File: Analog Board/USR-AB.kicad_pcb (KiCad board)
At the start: 2 copper layers, 81.3 x 8.9 mm, 6 parts, among them J2 S5B-XH-A_LF__SN_, J3 S5B-XH-A_LF__SN_, U2 CD74HC4067SM96, U3 SC0918

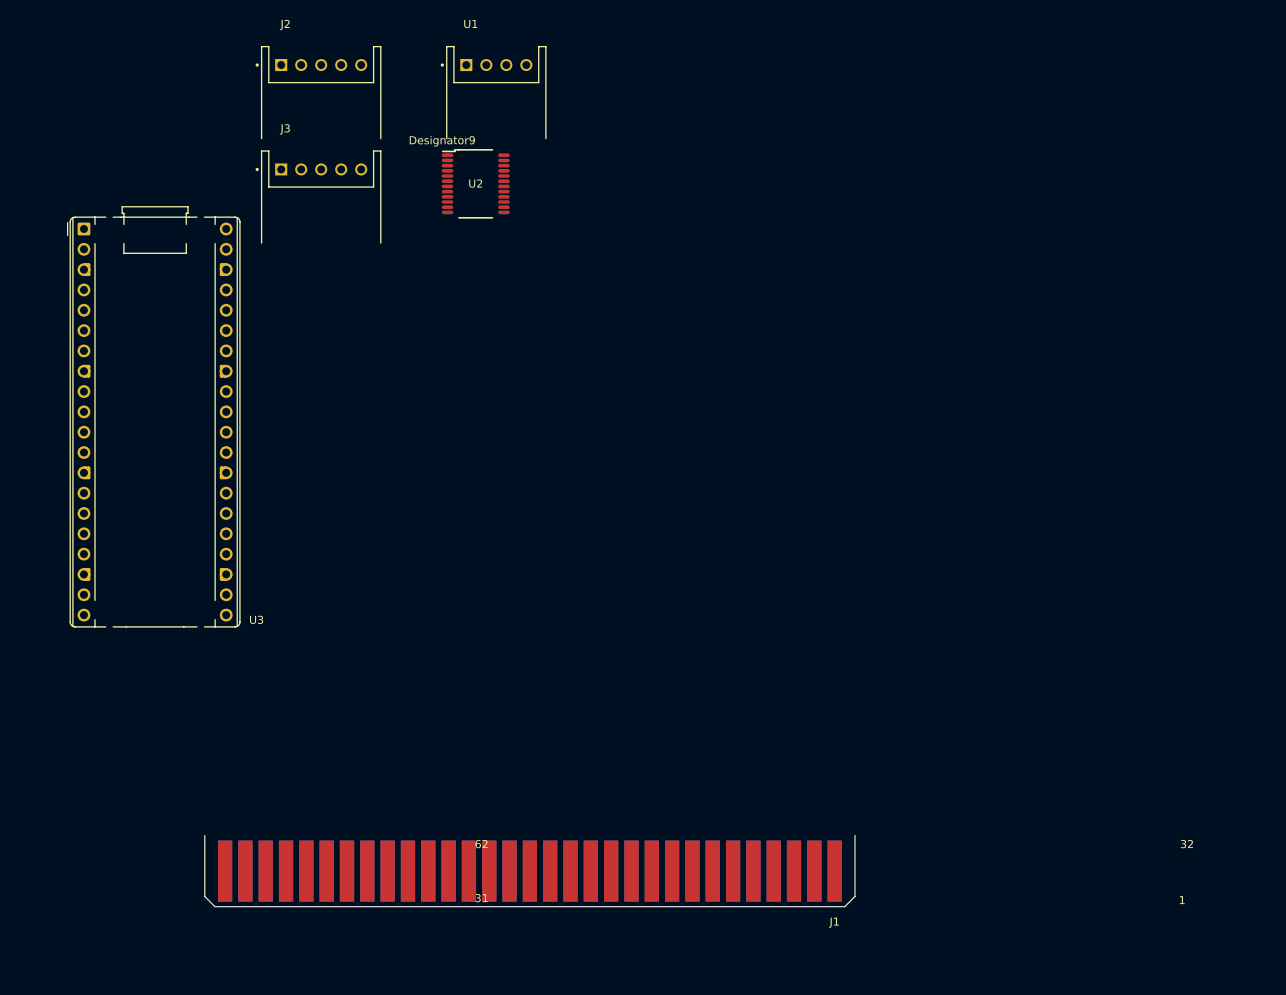
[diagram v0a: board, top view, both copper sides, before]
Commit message: updated Analog board PCB
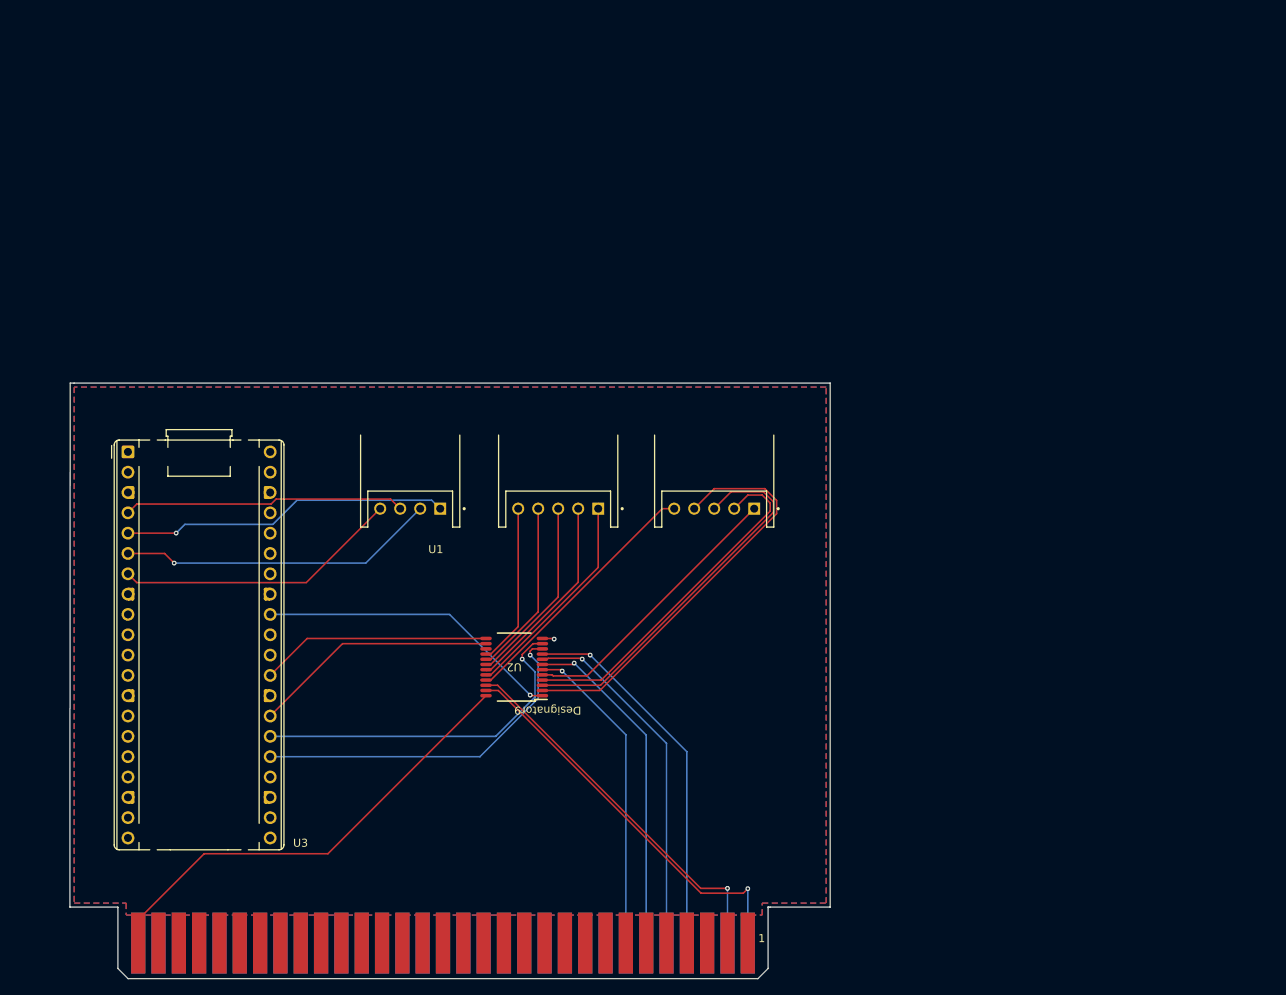
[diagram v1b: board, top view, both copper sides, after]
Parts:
- moved J2 66.0 mm to (125.5, 90.0), turned to 180 degrees
- moved U2 60.6 mm to (100.5, 115.5), turned to 180 degrees
- moved U1 45.4 mm to (87.5, 90.0), turned to 180 degrees
- moved J3 42.9 mm to (106.0, 90.0), turned to 180 degrees
- moved U3 28.4 mm to (52.2, 88.6)
- moved J1 14.1 mm to (129.7, 150.0)
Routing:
- net 5V: track 0.00 -> 58.0 mm
- net M4_THERM: track 0.00 -> 52.6 mm
- net DRIVE1_HE: track 0.00 -> 50.3 mm, vias 0 -> 1
- net M3_THERM: track 0.00 -> 48.5 mm
- net DRIVE2_HE: track 0.00 -> 47.5 mm, vias 0 -> 1
- net M1_CS: track 0.00 -> 47.0 mm, vias 0 -> 1
- net M2_CS: track 0.00 -> 44.9 mm, vias 0 -> 1
- net MUX_S0: track 0.00 -> 44.5 mm, vias 0 -> 1
- net M2_THERM: track 0.00 -> 44.4 mm
- net MUX_S1: track 0.00 -> 44.2 mm, vias 0 -> 1
- net M3_CS: track 0.00 -> 42.8 mm, vias 0 -> 1
- net PDB_Din: track 0.00 -> 41.2 mm, vias 0 -> 1
- net M4_CS: track 0.00 -> 39.8 mm, vias 0 -> 1
- net PDB_Dout: track 0.00 -> 39.8 mm, vias 0 -> 1
- net MUX_out: track 0.00 -> 38.2 mm, vias 0 -> 1
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- added copper zone on B.Cu, net GND
- added copper zone on F.Cu, net GND
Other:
- board size 81.3 x 8.9 mm -> 95 x 65.6 mm

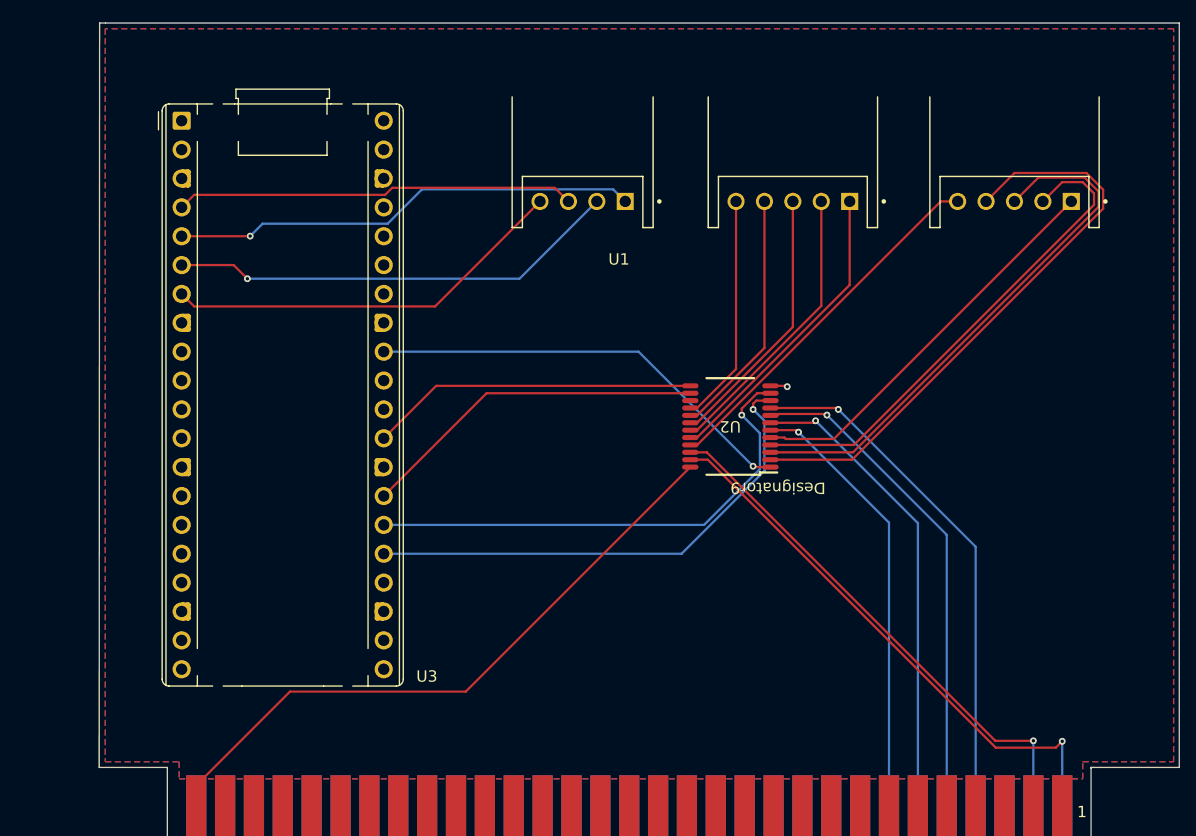
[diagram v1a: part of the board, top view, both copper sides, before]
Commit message: Added silkscreen labels to edge connectors
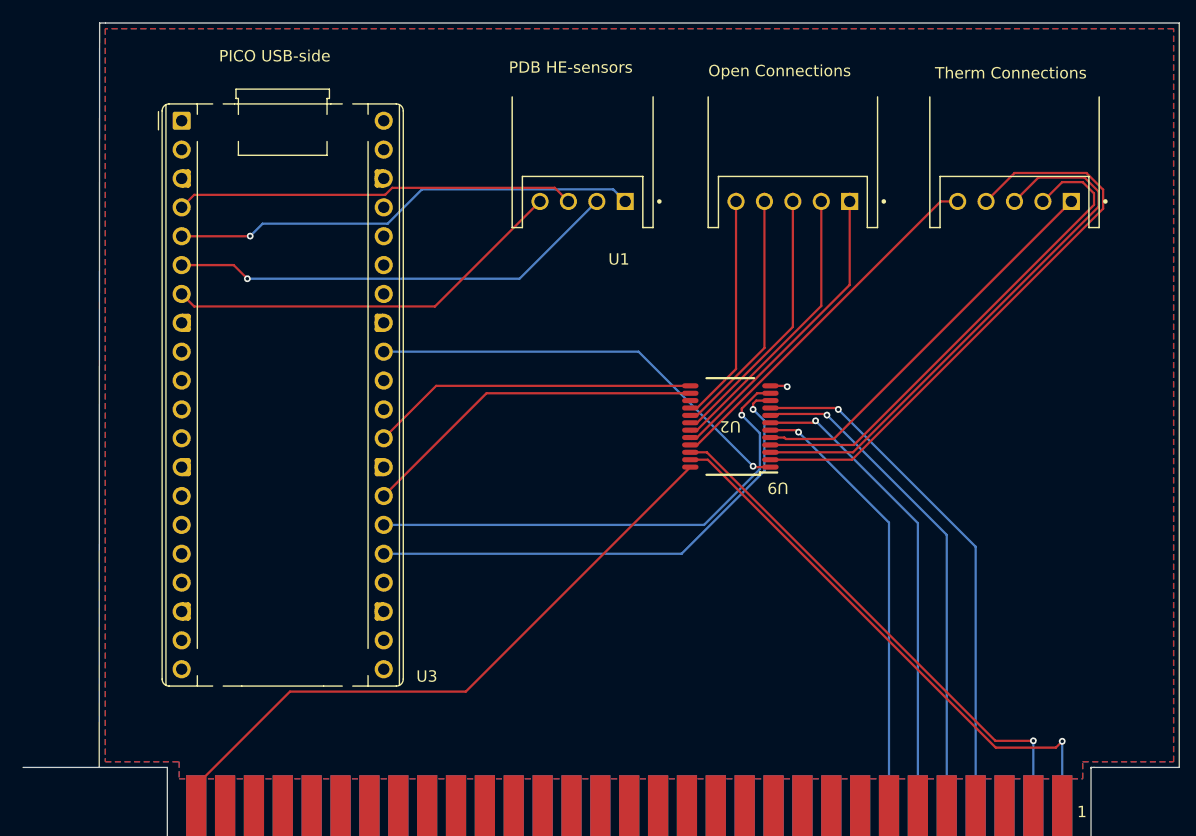
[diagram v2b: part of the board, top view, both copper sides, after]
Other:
- board size 95 x 65.6 mm -> 101.7 x 65.6 mm
- board text added: "Open Connections"
- board text added: "PDB HE-sensors"
- board text added: "PICO USB-side"
- board text added: "Therm Connections"
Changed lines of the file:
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@@
 			(layer "F.Fab")
 		)
-		(fp_text user "Designator9"
+		(fp_text user "U9"
 			(at -4.191 -5.4102 180)
 			(unlocked yes)
@@
 	(gr_line
 		(start 50.96 145.5)
-		(end 44.96 145.5)
+		(end 38.26 145.5)
 		(stroke
 			(width 0.05)
-			(type default)
+			(type solid)
 		)
 		(layer "Edge.Cuts")
@@
 		(layer "Edge.Cuts")
 	)
+	(gr_text "Therm Connections"
+		(at 118.5 85 0)
+		(layer "F.SilkS")
+		(effects
+			(font
+				(size 1 1)
+				(thickness 0.1)
+			)
+			(justify left bottom)
+		)
+	)
+	(gr_text "PDB HE-sensors"
+		(at 81 84.5 0)
+		(layer "F.SilkS")
+		(effects
+			(font
+				(size 1 1)
+				(thickness 0.1)
+			)
+			(justify left bottom)
+		)
+	)
+	(gr_text "Open Connections"
+		(at 98.55 84.803002 0)
+		(layer "F.SilkS")
+		(effects
+			(font
+				(size 1 1)
+				(thickness 0.1)
+			)
+			(justify left bottom)
+		)
+	)
+	(gr_text "PICO USB-side"
+		(at 55.5 83.5 0)
+		(layer "F.SilkS")
+		(effects
+			(font
+				(size 1 1)
+				(thickness 0.1)
+			)
+			(justify left bottom)
+		)
+	)
 	(segment

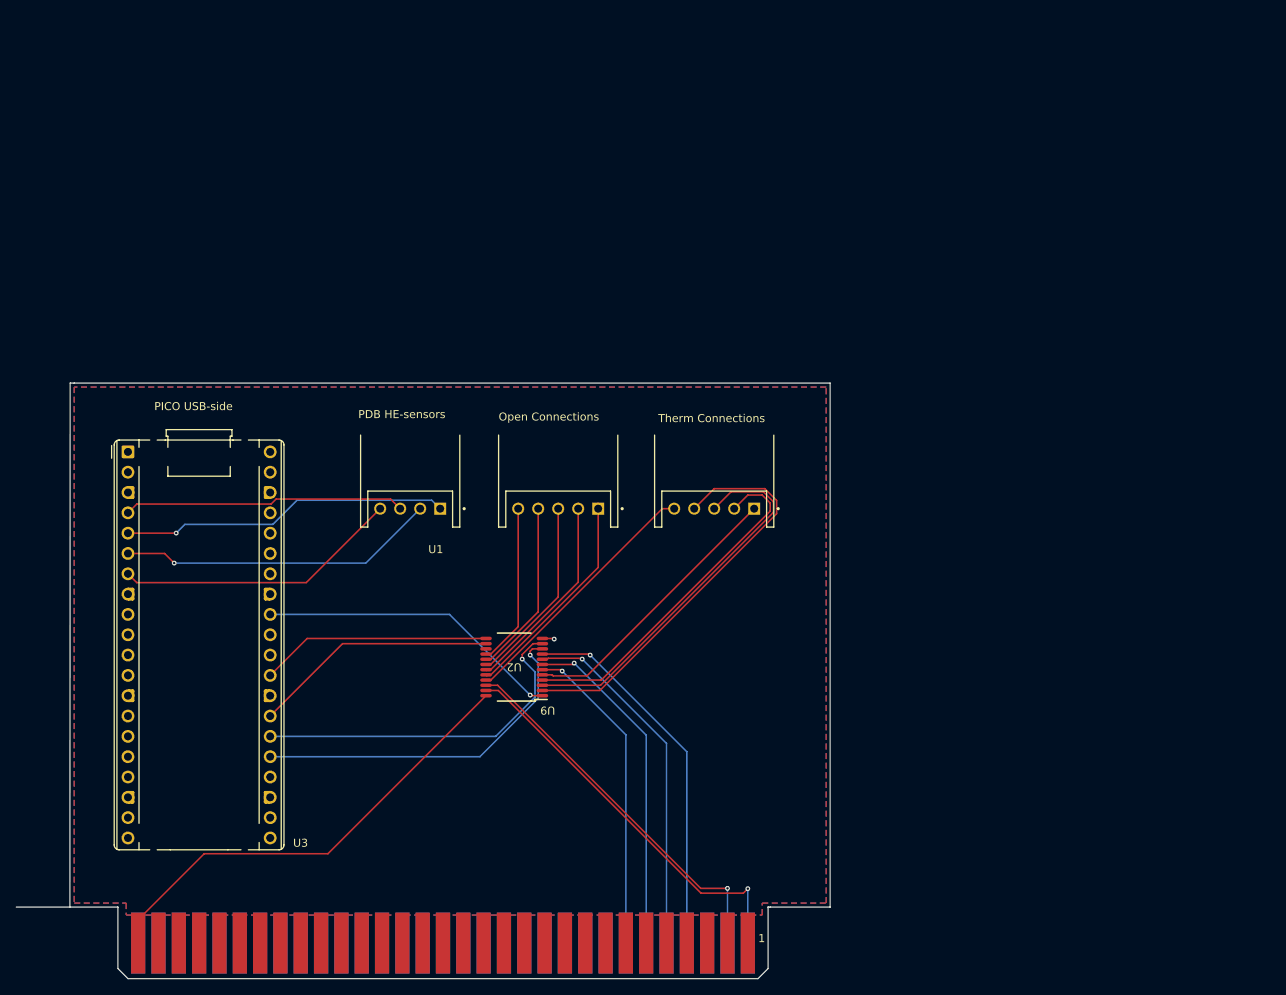
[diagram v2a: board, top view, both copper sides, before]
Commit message: Finished Analog board PCB
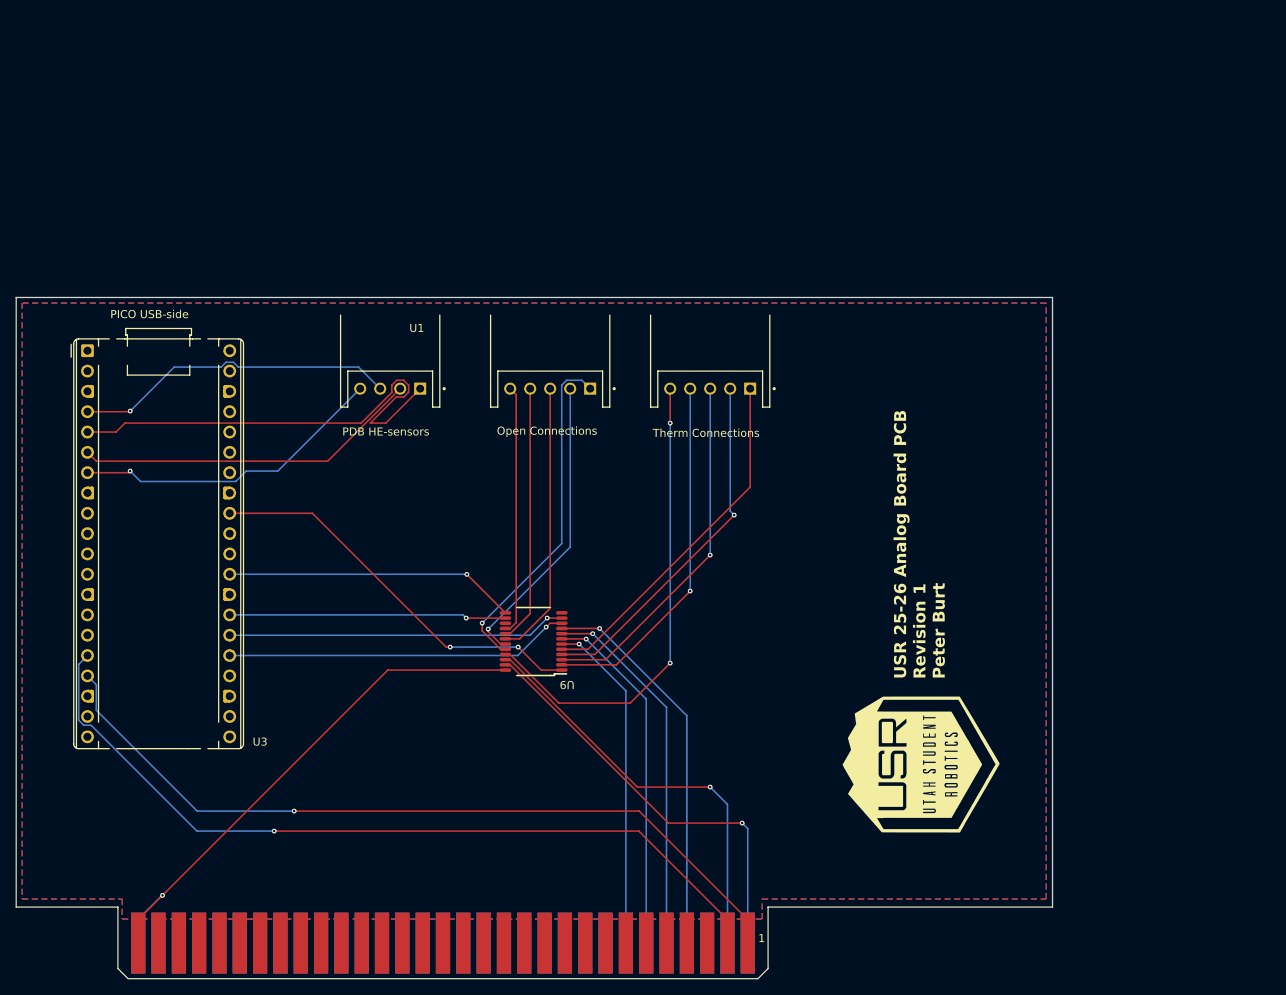
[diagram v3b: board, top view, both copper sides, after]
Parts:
- moved U1 15.2 mm to (85.0, 75.0)
- moved J3 15.0 mm to (105.0, 75.0)
- moved J2 15.0 mm to (125.0, 75.0)
- moved U3 13.6 mm to (47.2, 76.0)
- moved U2 4.02 mm to (102.9, 112.3)
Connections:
- J1 pad 1: UART_TX -> UART_TX-(host)
- J1 pad 2: UART_RX -> UART_RX-(host)
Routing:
- net UART_RX-(host): track 0.00 -> 102.9 mm, vias 0 -> 1
- net UART_TX-(host): track 0.00 -> 99.9 mm, vias 0 -> 1
- net AMB_THERM: track 33.0 -> 59.5 mm, vias 0 -> 2
- net PDB_Din: track 41.2 -> 58.9 mm, vias 1 -> 0
- net Connection_1: track 27.8 -> 42.9 mm, vias 0 -> 1
- net MUX_out: track 38.2 -> 49.6 mm, vias 1 -> 2
- net Connection_2: track 26.1 -> 37.4 mm, vias 0 -> 1
- net 5V: track 58.0 -> 69.0 mm, vias 0 -> 1
- net Connection_3: track 24.3 -> 34.6 mm
- net Connection_5: track 20.9 -> 31.2 mm
- net Connection_4: track 22.6 -> 32.3 mm
- net M1_THERM: track 35.8 -> 44.2 mm
- net MUX_S3: track 28.9 -> 36.5 mm, vias 0 -> 1
- net M4_THERM: track 52.6 -> 45.2 mm, vias 0 -> 1
- net PDB_CLK: track 35.2 -> 40.5 mm, vias 0 -> 1
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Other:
- board size 101.7 x 65.6 mm -> 129.5 x 76.3 mm
- board text added: "USR 25-26 Analog Board PCB Revision 1 Peter Burt"

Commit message: [Analog Board] added power to PICO, updated board dimensions
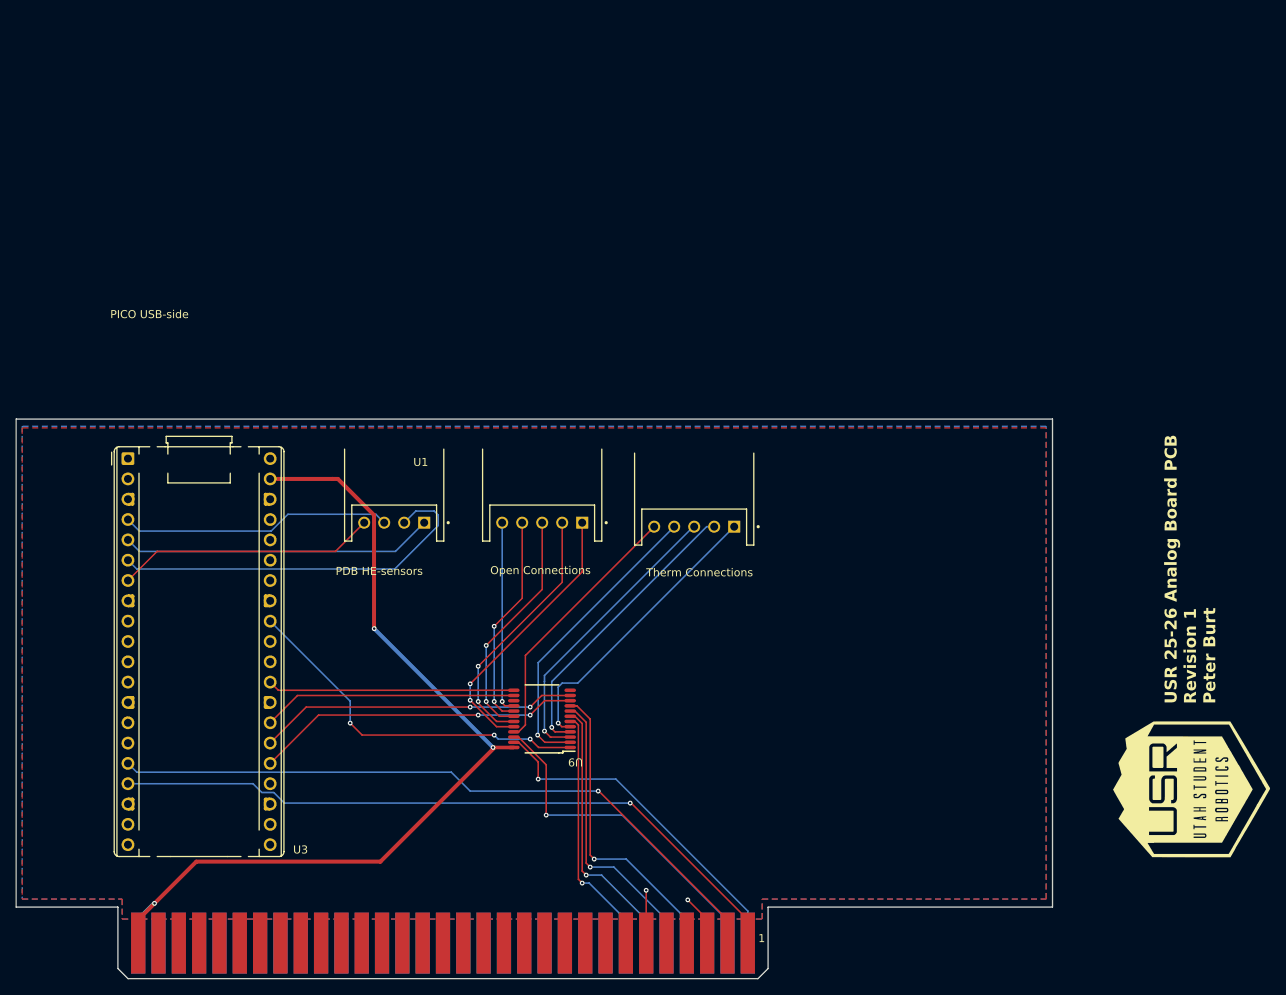
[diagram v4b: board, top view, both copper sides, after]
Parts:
- moved J2 17.4 mm to (123.0, 92.2)
- moved J3 16.8 mm to (104.0, 91.8)
- moved U1 16.8 mm to (85.5, 91.8)
- moved U3 14.4 mm to (52.2, 89.4)
- moved U2 9.73 mm to (104.0, 122.0)
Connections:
- U3 pad 39: unconnected-(U3-VSYS-Pad39) -> 5V
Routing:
- net 5V: track 69.0 -> 114.7 mm, vias 1 -> 3
- net AMB_THERM: track 59.5 -> 33.3 mm, vias 2 -> 0
- net PDB_Din: track 58.9 -> 39.1 mm
- net UART_RX-(host): track 102.9 -> 86.0 mm
- net GND: track 0.00 -> 13.0 mm, vias 0 -> 2
- net UART_TX-(host): track 99.9 -> 87.4 mm
- net M4_CS: track 42.0 -> 31.4 mm
- net M3_CS: track 44.2 -> 33.8 mm
- net M2_CS: track 46.4 -> 36.1 mm
- net M1_CS: track 48.6 -> 38.5 mm
- net DRIVE2_HE: track 52.6 -> 42.7 mm
- net DRIVE1_HE: track 53.1 -> 43.3 mm
- net Connection_1: track 42.9 -> 34.8 mm, vias 1 -> 2
- net M2_THERM: track 44.8 -> 36.8 mm
- net M1_THERM: track 44.2 -> 36.5 mm, vias 0 -> 1
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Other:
- board size 129.5 x 76.3 mm -> 129.5 x 61.1 mm
- board text added: "shorten height of the board"
